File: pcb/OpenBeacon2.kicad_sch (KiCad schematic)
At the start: 64 parts, among them J1 Bias V, J10 UART, J11 BNC, J2 PAI+, J3 PAI-, J4 Digital IO, J5 ADC Inputs, J6 SMA, J8 I2C Bus, J9 GND, Q1 2N7002, Q2 MMBT4403, Q3 2SK3074, Q4 2N7002, Q5 2N7002, U1 TLV61046A, U2 ASTX-H11-25.000MHZ-T, U3 SN74LVC1G17, U4 SI5351A, U5 MCP4725A1T-E/CH, U6 128x32 OLED, U7 Empyrean, U8 24AA64T

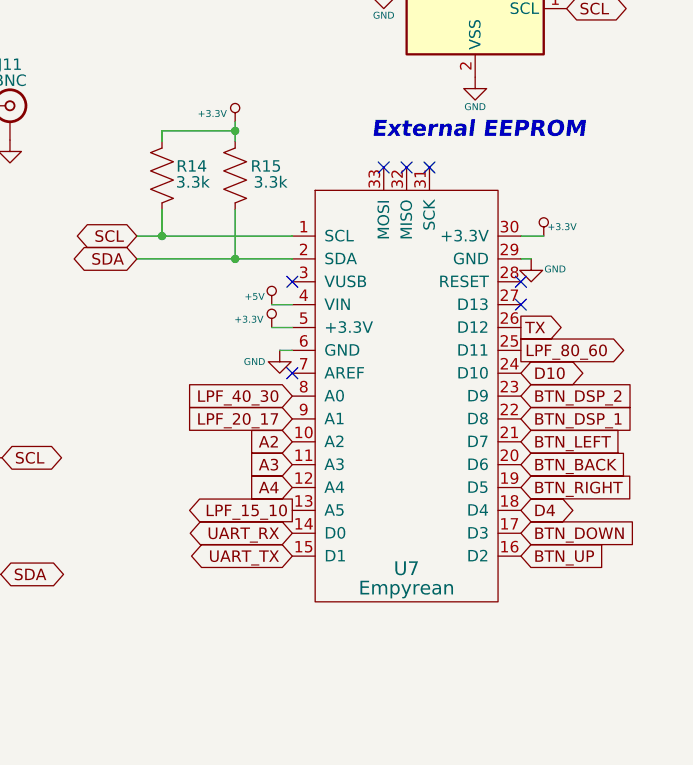
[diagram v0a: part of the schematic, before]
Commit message: Replace Empyrean SAMD21 module with AVR128DA32 + CP2102N USB-C/UPDI (from Si5351AVFO)
- New sheet mcu_usb: AVR128DA32-I/PT, 32.768k crystal on PF0/PF1 with 15p loads,
  USB-C + SP0503 ESD, CP2102N with DTR auto-reset, LP2985-3.3, UPDI header
- Remove U7 Empyrean from root sheet
- Relay drivers Q6-Q9: 2N7002 -> AO3400A for 3.3 V gate drive
- ERC 0 errors; schematic PDF regenerated; docs/VERIFY.md open items
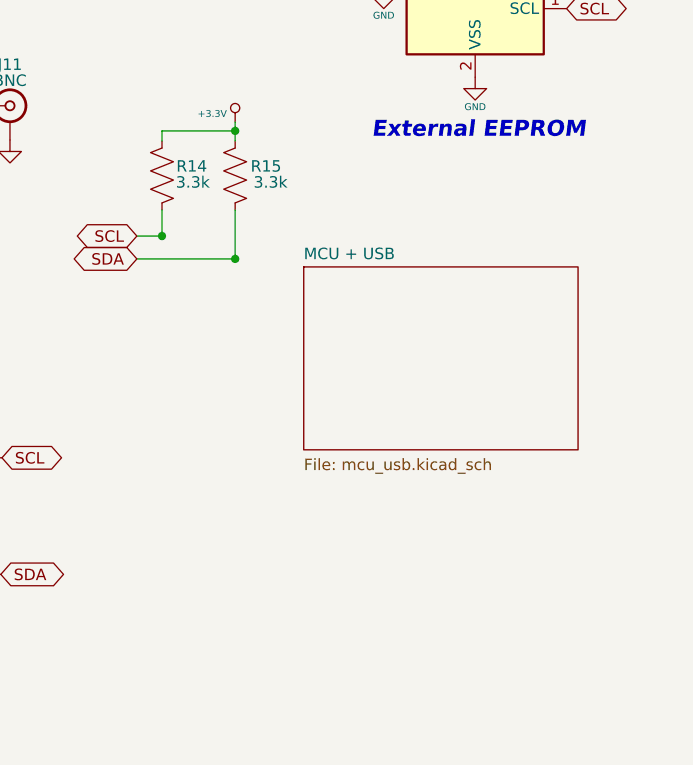
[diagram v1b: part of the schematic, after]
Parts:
- removed U7: Empyrean, EtherkitKicadLibrary:Empyrean, symbol EtherkitKicadLibrary:Empyrean
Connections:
- no-connect marks 9 -> 2
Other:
- added sheet MCU + USB (mcu_usb.kicad_sch)

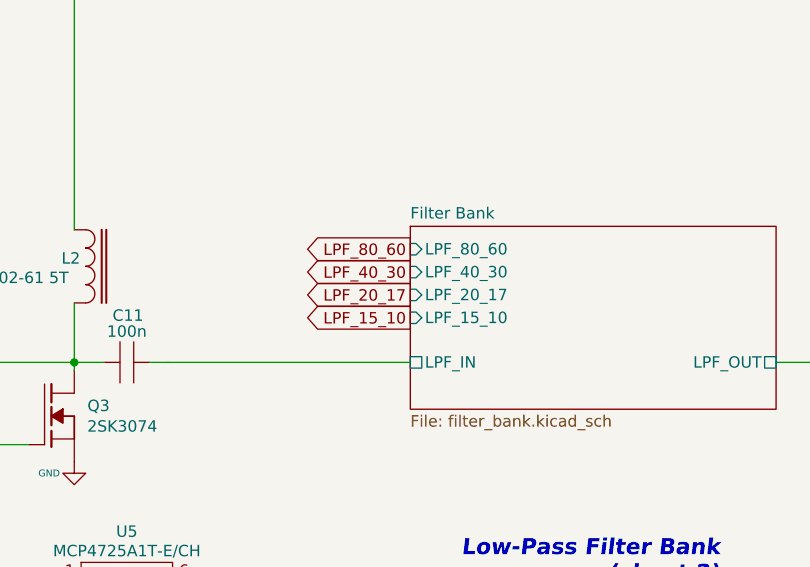
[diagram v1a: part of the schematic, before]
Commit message: Filter bank: 6-relay two-level tree driven by BAND_A/BAND_B
Replace the 8-relay, 4-driver bank with a 2-bit tree (K1-K3 input,
K4-K6 output, one G6K pole each). All relays off selects 80/60 m.
Q6/Q7 AO3400A drive the first and second levels; PA7/PC2 freed.
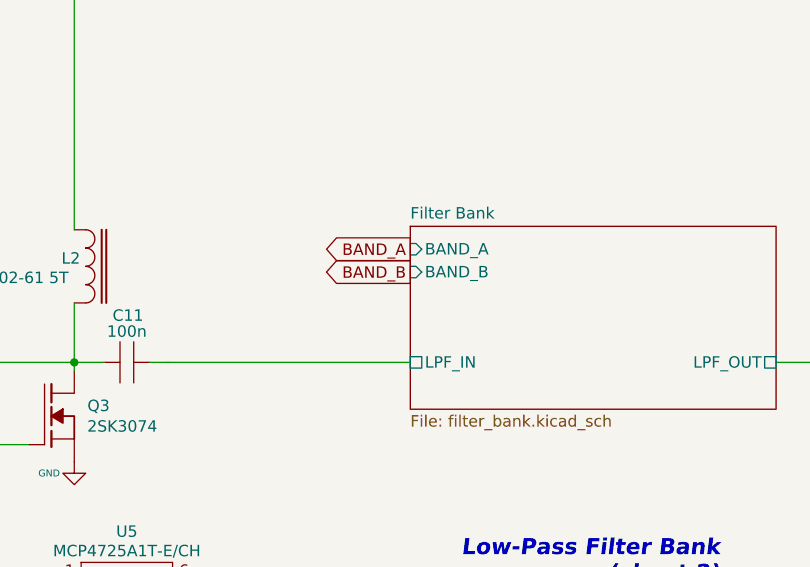
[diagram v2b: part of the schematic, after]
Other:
- sheet Filter Bank ports: added BAND_A, BAND_B; removed LPF_15_10, LPF_20_17, LPF_40_30, LPF_80_60
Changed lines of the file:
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@@
 		)
 	)
-	(global_label "LPF_80_60"
+	(global_label "BAND_A"
 		(shape output)
 		(at 125.73 101.60 180)
@@
 		)
 	)
-	(global_label "LPF_40_30"
+	(global_label "BAND_B"
 		(shape output)
 		(at 125.73 104.14 180)
@@
 		(property "Intersheetrefs" "${INTERSHEET_REFS}"
 			(at 125.73 104.14 0)
-			(effects
-				(font
-					(size 1.27 1.27)
-				)
-				(hide yes)
-			)
-		)
-	)
-	(global_label "LPF_20_17"
-		(shape output)
-		(at 125.73 106.68 180)
-		(fields_autoplaced yes)
-		(effects
-			(font
-				(size 1.27 1.27)
-			)
-			(justify right)
-		)
-		(property "Intersheetrefs" "${INTERSHEET_REFS}"
-			(at 125.73 106.68 0)
-			(effects
-				(font
-					(size 1.27 1.27)
-				)
-				(hide yes)
-			)
-		)
-	)
-	(global_label "LPF_15_10"
-		(shape output)
-		(at 125.73 109.22 180)
-		(fields_autoplaced yes)
-		(effects
-			(font
-				(size 1.27 1.27)
-			)
-			(justify right)
-		)
-		(property "Intersheetrefs" "${INTERSHEET_REFS}"
-			(at 125.73 109.22 0)
 			(effects
 				(font
@@
 			)
 		)
-		(pin "LPF_80_60" input
+		(pin "BAND_A" input
 			(at 125.73 101.60 180)
 			(effects
@@
 			)
 		)
-		(pin "LPF_40_30" input
+		(pin "BAND_B" input
 			(at 125.73 104.14 180)
 			(effects
 				(font
-					(size 1.27 1.27)
-				)
-				(justify left)
-			)
-		)
-		(pin "LPF_20_17" input
-			(at 125.73 106.68 180)
-			(effects
-				(font
-					(size 1.27 1.27)
-				)
-				(justify left)
-			)
-		)
-		(pin "LPF_15_10" input
-			(at 125.73 109.22 180)
-			(effects
-				(font

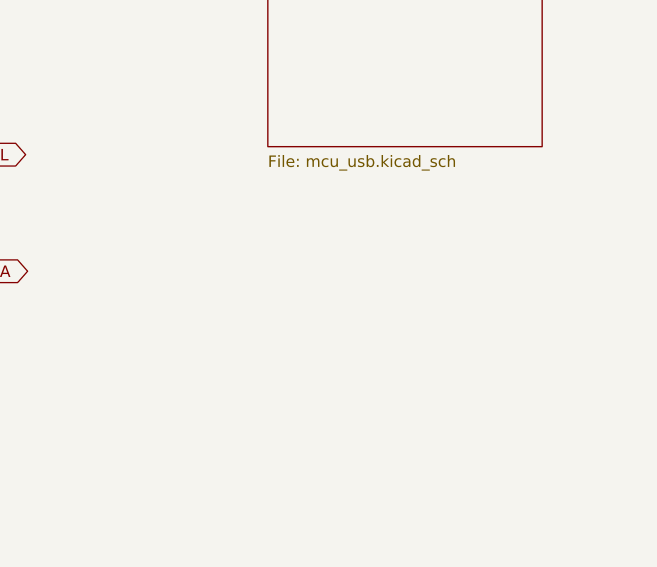
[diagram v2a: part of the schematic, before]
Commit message: Add GPS option sheet (u-blox MAX-M10S) on USART2 ALT1
- New pcb/gps.kicad_sch: MAX-M10S U12 on +3.3V (VIO_SEL open), UART to
  PF4/PF5, TIMEPULSE via 470R to GPS_PPS / J14, active-antenna bias-T
  (10R, 10n, 27nH per IM 4.3.4) to U.FL J15, supercap V_BCKP via
  1N5711W + 1k.
- MCU: D4 moved PF4 -> PA7, sync LED moved PF5 -> PC2.
- GPS_PPS MCU pin left open; options in VERIFY.md.
- Regenerated schematic PDF; ERC 0 errors.
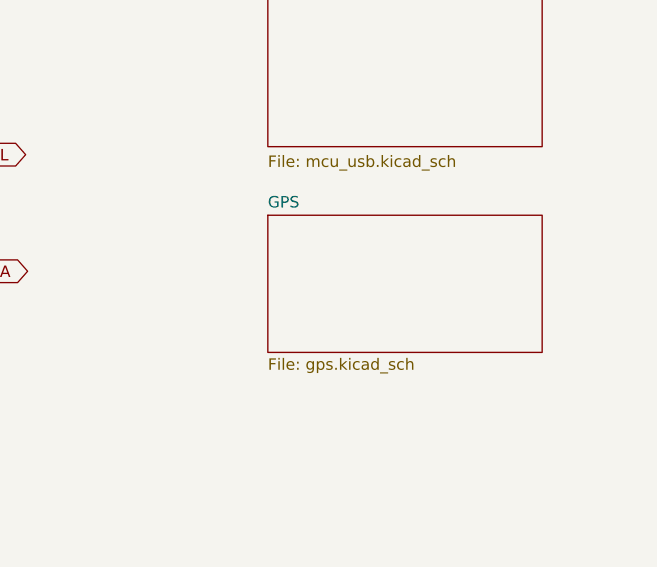
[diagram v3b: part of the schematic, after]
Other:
- added sheet GPS (gps.kicad_sch)
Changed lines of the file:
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@@
+		)
+	)
+	(sheet
+		(at 228.6 160.02)
+		(size 30.48 15.24)
+		(exclude_from_sim no)
+		(in_bom yes)
+		(on_board yes)
+		(dnp no)
+		(fields_autoplaced no)
+		(stroke
+			(width 0.1524)
+			(type solid)
+		)
+		(fill
+			(color 0 0 0 0.0000)
+		)
+		(property "Sheetname" "GPS"
+			(at 228.6 159.31 0)
+			(effects
+				(font
+					(size 1.27 1.27)
+				)
+				(justify left bottom)
+			)
+		)
+		(property "Sheetfile" "gps.kicad_sch"
+			(at 228.6 175.86 0)
+			(effects
+				(font
+					(size 1.27 1.27)
+				)
+				(justify left top)
+			)
+		)
+		(instances
+			(project "OpenBeacon2"
+				(path "/046319a3-a6ce-4e59-a888-94e340127381"
+					(page "4")
+				)
+			)
 		)
 	)

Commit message: Root sheet: redraw page 1 in rev C style (gen_main.py), A3, grouped blocks, Si5351A synth as a self-contained swap block
kicad-cli netlist before/after: 149/149 nets with identical pin sets; 17 auto-named nets
got readable labels (e.g. Net-(Q3-D) -> PA_DRAIN). No component, value or footprint changes.
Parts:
- removed C1, C10, C11, C14, C17, C18, C19, C20, C21, C22, C23, C24, C5, C6, C8: 100n, Capacitor_SMD:C_0805_2012Metric, symbol EtherkitKicadLibrary:C
- removed C2: 4.7u, Capacitor_SMD:C_0805_2012Metric, symbol EtherkitKicadLibrary:C
- removed C3: 10u, Capacitor_SMD:C_0805_2012Metric, symbol EtherkitKicadLibrary:C
- removed C4: 10n, Capacitor_SMD:C_0805_2012Metric, symbol EtherkitKicadLibrary:C
- removed C7, C9: 1u, Capacitor_SMD:C_0805_2012Metric, symbol EtherkitKicadLibrary:C
- removed R1, R2, R3: 22k, Resistor_SMD:R_0805_2012Metric, symbol EtherkitKicadLibrary:R
- removed R11, R12, R14, R15, R5: 3.3k, Resistor_SMD:R_0805_2012Metric, symbol EtherkitKicadLibrary:R
- removed R6: 10, Resistor_SMD:R_0805_2012Metric, symbol EtherkitKicadLibrary:R
- removed R7: 56, Resistor_SMD:R_0805_2012Metric, symbol EtherkitKicadLibrary:R
- removed R8: 1 1%, Resistor_SMD:R_0805_2012Metric, symbol EtherkitKicadLibrary:R
- added C1, C10, C11, C14, C17, C18, C19, C20, C21, C22, C23, C24, C5, C6, C8: 100n, Capacitor_SMD:C_0805_2012Metric, symbol Device:C_Small
- added C2: 4.7u, Capacitor_SMD:C_0805_2012Metric, symbol Device:C_Small
- added C3: 10u, Capacitor_SMD:C_0805_2012Metric, symbol Device:C_Small
- added C4: 10n, Capacitor_SMD:C_0805_2012Metric, symbol Device:C_Small
- added C7, C9: 1u, Capacitor_SMD:C_0805_2012Metric, symbol Device:C_Small
- added R1, R2, R3: 22k, Resistor_SMD:R_0805_2012Metric, symbol Device:R_Small_US
- added R11, R12, R14, R15, R5: 3.3k, Resistor_SMD:R_0805_2012Metric, symbol Device:R_Small_US
- added R6: 10, Resistor_SMD:R_0805_2012Metric, symbol Device:R_Small_US
- added R7: 56, Resistor_SMD:R_0805_2012Metric, symbol Device:R_Small_US
- added R8: 1 1%, Resistor_SMD:R_0805_2012Metric, symbol Device:R_Small_US
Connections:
- net +3.3V: now also C14.1, C22.1, C6.1, R14.1, R15.1
- net +5V: now also C1.1, C10.1, C2.1, R11.1, R12.1
- net BTN_BACK: now also C23.1
- net BTN_DOWN: now also C20.1
- net BTN_DSP_1: now also C17.1
- net BTN_DSP_2: now also C19.1
- net BTN_LEFT: now also C18.1
- net BTN_RIGHT: now also C24.1
- net BTN_UP: now also C21.1
- net GND: now also C1.2, C10.2, C14.2, C17.2, C18.2, C19.2, C2.2, C20.2, C21.2, C22.2, C23.2, C24.2, C3.2, C6.2, C7.2, C9.2, R1.2
- net SCL: now also R14.2
- net SCL_5V: now also R11.2
- net SDA: now also R15.2
- net SDA_5V: now also R12.2
- net TX: now also R1.1
- net TCXO_OUT: now reaches R4.1, U2.3 (OUT)
- net SI_XA: now reaches R4.2, U4.2 (XA)
- net CLK2_SMA: now reaches J6.1 (In), U4.6 (CLK2)
- net PA_DRIVE: now reaches U3.4
- net PA_DRIVE: now also C5.2, R5.2
- net PA_GATE: now reaches Q3.2 (G)
- net PA_GATE: now also C5.1, R7.1
- net PA_DRAIN: now reaches L2.2, Q3.3 (D)
- net PA_DRAIN: now also C11.2, C8.1
- net PA_BIAS: now reaches J1.1 (P1), U5.1 (VOUT)
- net PA_BIAS: now also C9.1, R7.2
- net TX_N: now reaches Q1.3 (D)
- net TX_N: now also R3.2
- net PAI_N: now reaches J3.1 (P1), L2.1
- net PAI_N: now also R8.1
- net VBOOST: now reaches Q2.1 (E), U1.5 (VO)
- net VBOOST: now also C3.1, R2.1
- net PA_SW_B: now reaches Q2.2 (B)
- net PA_SW_B: now also C4.2, R2.2, R3.1
- net PA_VDD: now reaches Q2.3 (C)
- net PA_VDD: now also C4.1, R6.2
- net PAI_P: now reaches J2.1 (P1)
- net PAI_P: now also C7.1, R6.1, R8.2
- net BOOST_SW: now reaches L1.1, U1.1 (SW)
- net Filter Bank/LPF_OUT renamed LPF_OUT
- new net LPF_IN: C11.1
- new net PA_FB: C8.2, R5.1
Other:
- note added: "12 V boost (TLV61046A)"
- note added: "I/O headers"
- note added: "I2C 3.3 V <-> 5 V level shift (OLED, DAC) + 24AA64 EEPROM"
- note added: "Only interface to the rest of the board: +3.3V, GND, SCL/SDA, CLK0 (to U3 buffer), CLK2_SMA (J6)."
- note added: "PAI+/PAI- = PA current-sense test points across R8 (1 ohm)."
- note added: "Power amplifier (2SK3074) + bias DAC (MCP4725)"
- note added: "Sub-sheets: Filter Bank (LPF_IN/LPF_OUT, BAND_A/B), MCU + USB (AVR128DA48, CP2102N, 3.3 V), GPS (MAX-M10S). They connect through the global labels."
- note added: "Synth: Si5351A + 25 MHz TCXO (self-contained swap block)"
- note added: "TX keying + PA supply switch"
- note added: "U1 FB tied to VIN = fixed 12 V output (TLV61046A DS). C2 input, C3 output, both beside U1."
- note added: "User interface: OLED + buttons (100n debounce beside each button)"
- note removed: "Boost Converter"
- note removed: "External EEPROM"
- note removed: "I2C Level Conversion"
- note removed: "IO Headers"
- note removed: "Keying"
- note removed: "Low-Pass Filter Bank (sheet 2)"
- note removed: "PA Bias"
- note removed: "Power Amplifier"
- note removed: "Si5351A PLL"
- note removed: "User Interface"

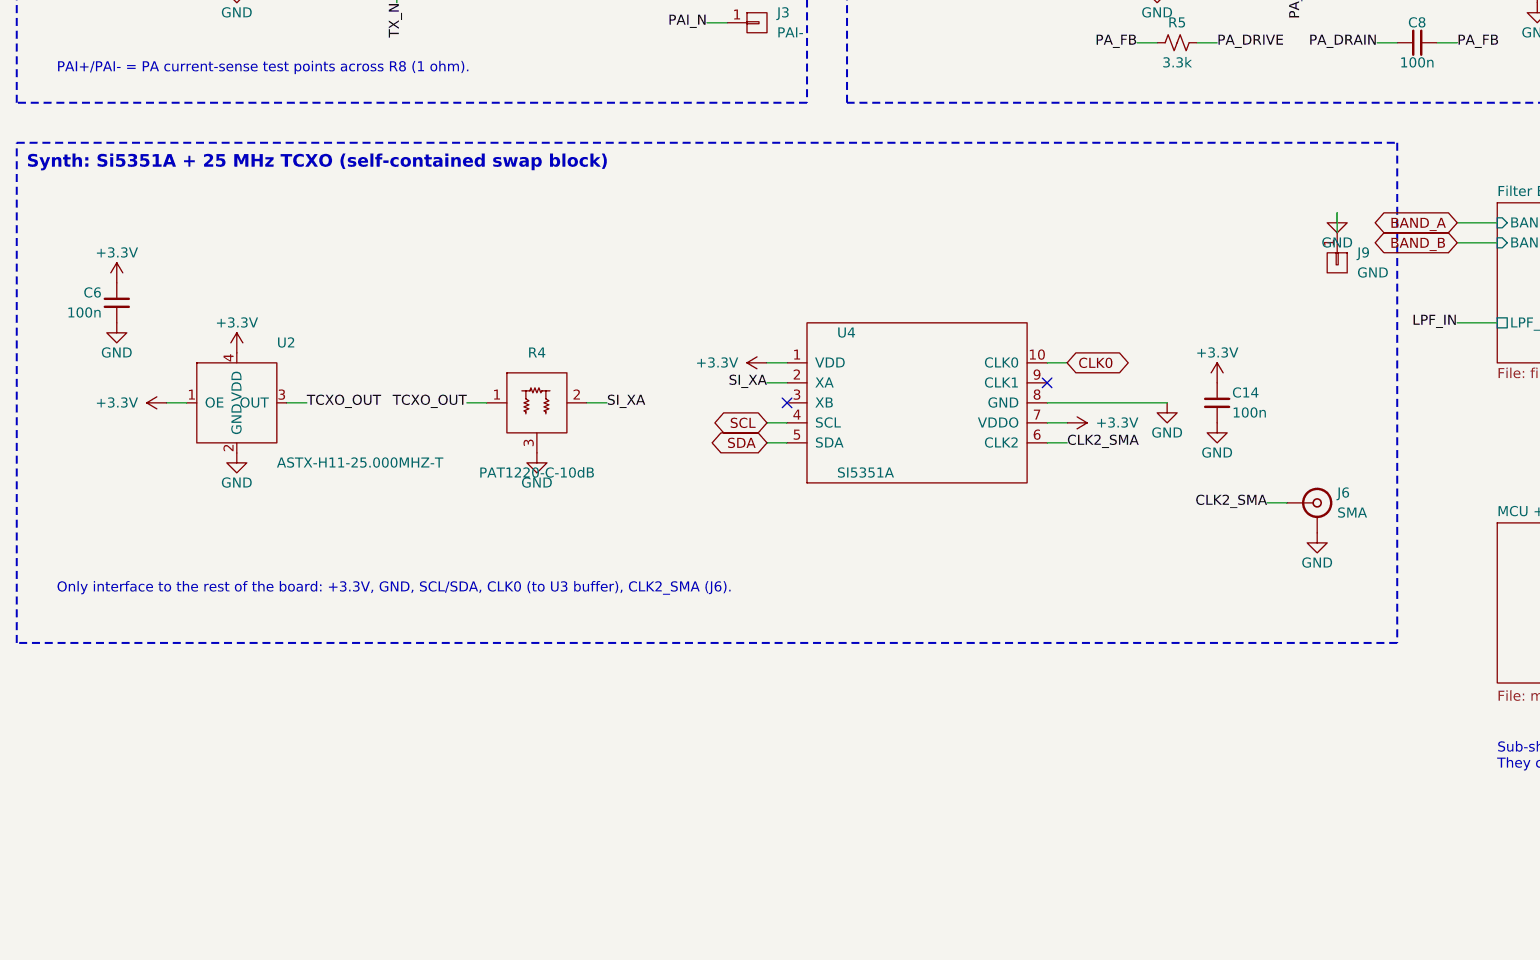
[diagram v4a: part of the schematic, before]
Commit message: Replace Si5351A with Si5351C; add SMA CLKIN and CAL_CLK to PB2
- U4 SI5351C-B-GMR (LCSC C2649375, alt SI5351C-B-GM C3608122), QFN-20 4x4 EP2.7, EP to GND
- TCXO stays on XA (XB open); CLK0 to PA buffer and CLK2 to J6 unchanged
- J16 BWSMA-KE-P001 (C496550) to CLKIN: 49.9R term, 100n AC coupling, 10k/10k VDD/2 bias
- CLK4 -> R47 33R -> CAL_CLK -> PB2 (EVSYS CH0/1); PPS stays on PF2 (CH4/5)
- OEB tied low; INTR 10k pull-up -> SI_INTR -> PB3
- 100n on VDD and each VDDOx (C14, C50-C53)
- VERIFY: Si5351C section, 10 s PPS-gated 32-bit TCB0/TCB1 cascade count
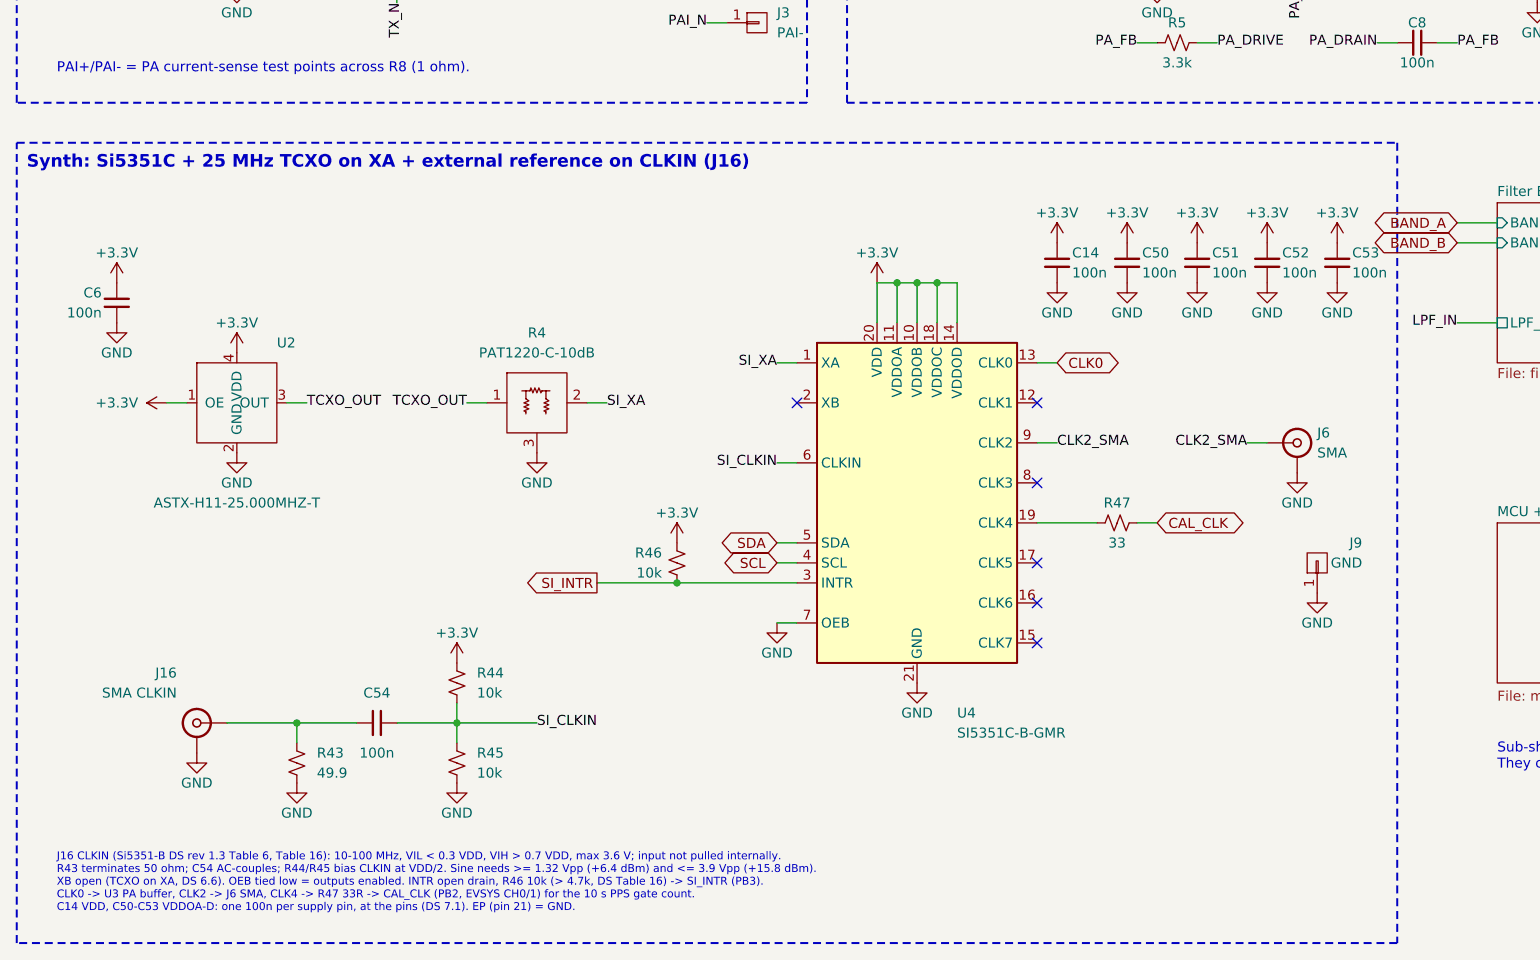
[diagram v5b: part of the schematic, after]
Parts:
- removed U4: SI5351A, EtherkitKicadLibrary:MSOP-10, symbol EtherkitKicadLibrary:SI5351A
- added C50, C51, C52, C53, C54: 100n, Capacitor_SMD:C_0603_1608Metric, symbol Device:C_Small
- added J16: SMA CLKIN, EtherkitKicadLibrary:SMA-ENDLAUNCH, symbol EtherkitKicadLibrary:BNC
- added R43: 49.9, Resistor_SMD:R_0603_1608Metric, symbol Device:R_Small_US
- added R44, R45, R46: 10k, Resistor_SMD:R_0603_1608Metric, symbol Device:R_Small_US
- added R47: 33, Resistor_SMD:R_0603_1608Metric, symbol Device:R_Small_US
- added U4: SI5351C-B-GMR, Package_DFN_QFN:QFN-20-1EP_4x4mm_P0.5mm_EP2.7x2.7mm, symbol Oscillator:Si5351C-B-GM
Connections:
- net +3.3V: now also C50.1, C51.1, C52.1, C53.1, R44.1, R46.1, U4.10 (VDDOB), U4.11 (VDDOA), U4.14 (VDDOD), U4.18 (VDDOC), U4.20 (VDD)
- net CLK0: now also U4.13 (CLK0)
- net CLK2_SMA: now also U4.9 (CLK2)
- net GND: now also C50.2, C51.2, C52.2, C53.2, J16.2 (Ext), R43.2, R45.2, U4.21 (GND), U4.7 (OEB)
- net SCL: now also U4.4 (SCL)
- net SDA: now also U4.5 (SDA)
- net SI_XA: now also U4.1 (XA)
- new net: C54.1, J16.1 (In), R43.1
- new net: R47.1, U4.19 (CLK4)
- new net CAL_CLK: R47.2
- new net SI_CLKIN: C54.2, R44.2, R45.1, U4.6 (CLKIN)
- new net SI_INTR: R46.2, U4.3 (INTR)
- no-connect marks 2 -> 6
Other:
- note added: "J16 CLKIN (Si5351-B DS rev 1.3 Table 6, Table 16): 10-100 MHz, VIL < 0.3 VDD, VIH > 0.7 VDD, max 3.6 V; input not pulled internally. R43 terminates 50 ohm; C54 AC-couples; R44/R45 bias CLKIN at VDD/2. Sine needs >= 1.32 Vpp (+6.4 dBm) and <= 3.9 Vpp (+15.8 dBm). XB open (TCXO on XA, DS 6.6). OEB tied low = outputs enabled. INTR open drain, R46 10k (> 4.7k, DS Table 16) -> SI_INTR (PB3). CLK0 -> U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"
- note added: "Synth: Si5351C + 25 MHz TCXO on XA + external reference on CLKIN (J16)"
- note removed: "Only interface to the rest of the board: +3.3V, GND, SCL/SDA, CLK0 (to U3 buffer), CLK2_SMA (J6)."
- note removed: "Synth: Si5351A + 25 MHz TCXO (self-contained swap block)"
